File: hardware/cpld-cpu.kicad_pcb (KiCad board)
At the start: 4 copper layers, 259.1 x 198.1 mm, 435 parts, among them J1 Acc, J10 Page, J11 PC_H, J12 Conn_02x14_Odd_Even, J13 GPIO, J14 Conn_02x17_Odd_Even, J15 Conn_01x07, J16 Clock, J2 X, J3 IR, J4 AXM, J5 Dec, J6 AR, J7 ALU, J8 Index, J9 PC_L, SW1 BTN0, SW10 Step 8, SW11 S1, SW12 S3, SW2 BTN1, SW3 BTN2, SW4 Halt, SW5 Reset, SW6 Step 1, SW7 S0, SW8 S2, SW9 S4, U1 Acc, U10 RAM_Page, U11 PC_H, U12 CY62138FV30LL, U13 GPIO_RNG, U14 Clock, U2 X, U3 IR, U4 Multiplexer, U5 Decoder, U6 AR, U7 ALU, U8 RAM_Index, U9 PC_L

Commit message: Add logos and version
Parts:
- added H1: MountingHole, Mounting_Holes:MountingHole_4.3mm_M4, F.Cu at (15.2, 203.2)
- added H2: MountingHole, Mounting_Holes:MountingHole_4.3mm_M4, F.Cu at (15.2, 15.2)
- added H3: MountingHole, Mounting_Holes:MountingHole_4.3mm_M4, F.Cu at (264.2, 15.2)
- added H4: MountingHole, Mounting_Holes:MountingHole_4.3mm_M4, F.Cu at (264.2, 203.2)
- added S1: KicadLogo, Symbols:Symbol_KiCAD-Logo_CopperAndSilkScreenTop, F.Cu at (255.3, 61.0)
- added S2: OSHWLogo, CPLD_CPU_Symbols:OSHW-Logo2_14.6x12mm_Copper_Top, F.Cu at (237.5, 62.2)
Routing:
- added copper zone on F.Cu, net (none)
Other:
- board text added: "CPLD CPU"
- board text added: "https://github.com/jimmo/cpld-cpu/"
- board text added: "v1.0 2018-12-20"

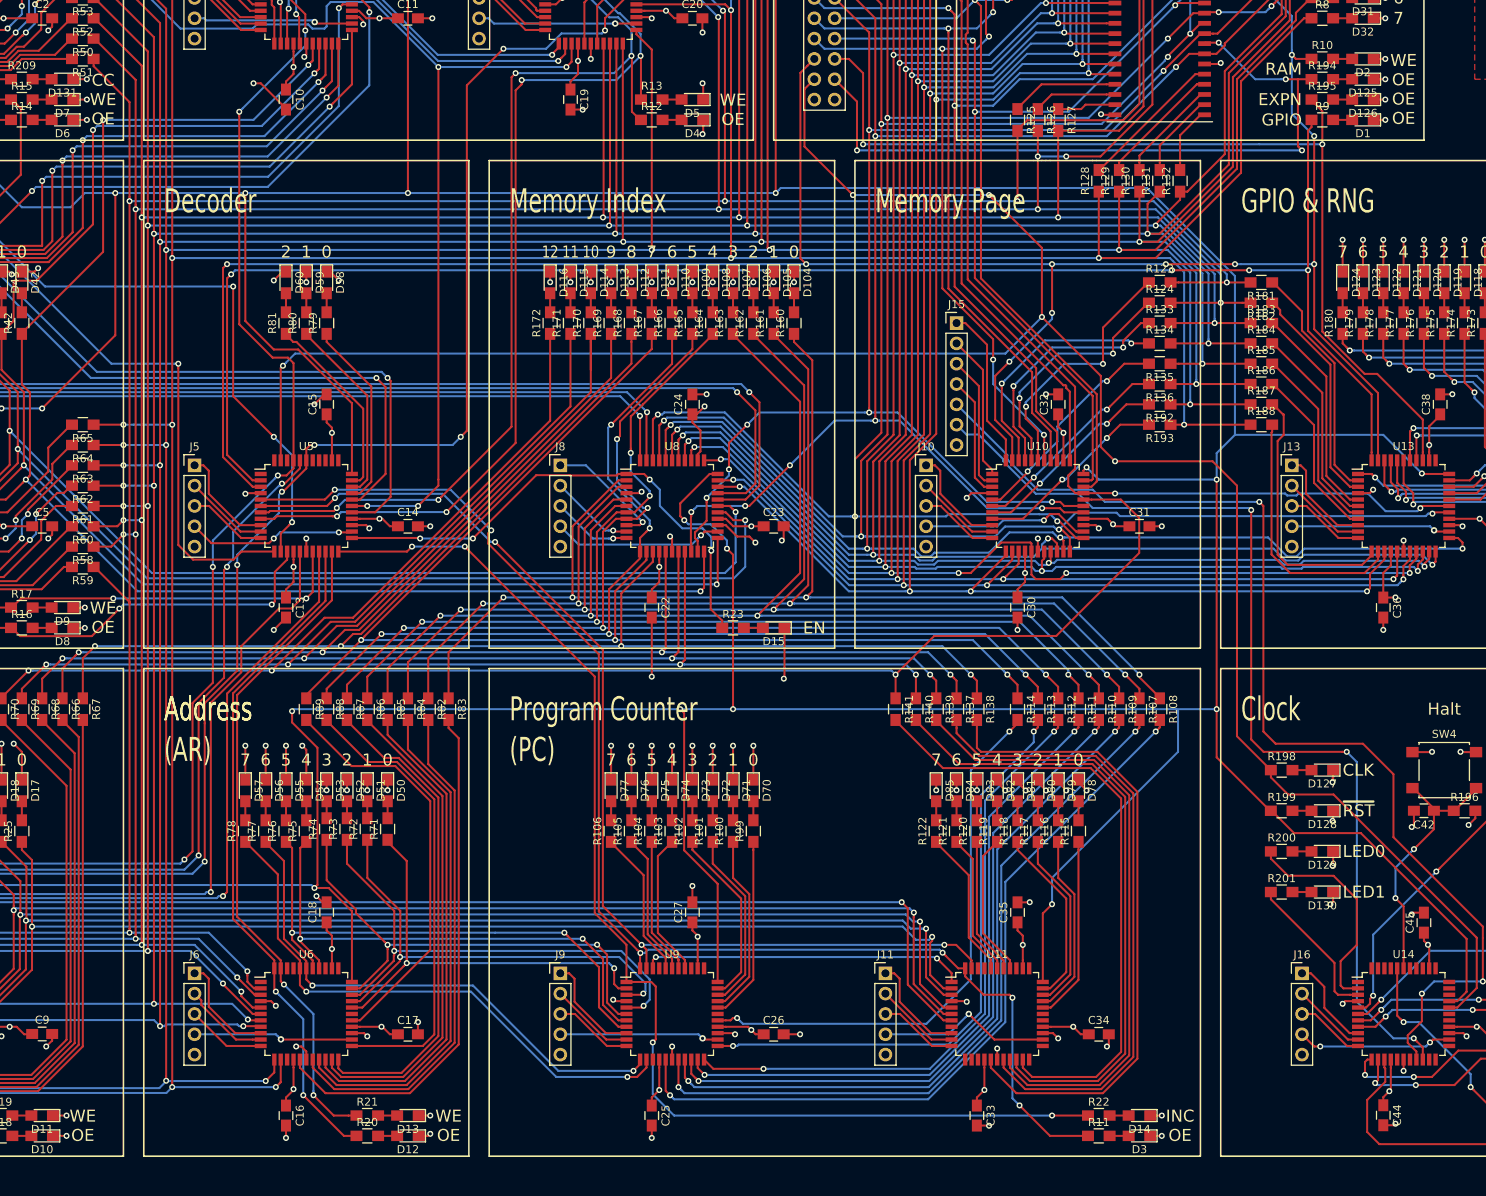
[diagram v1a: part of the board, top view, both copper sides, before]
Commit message: Name inverted nets correctly
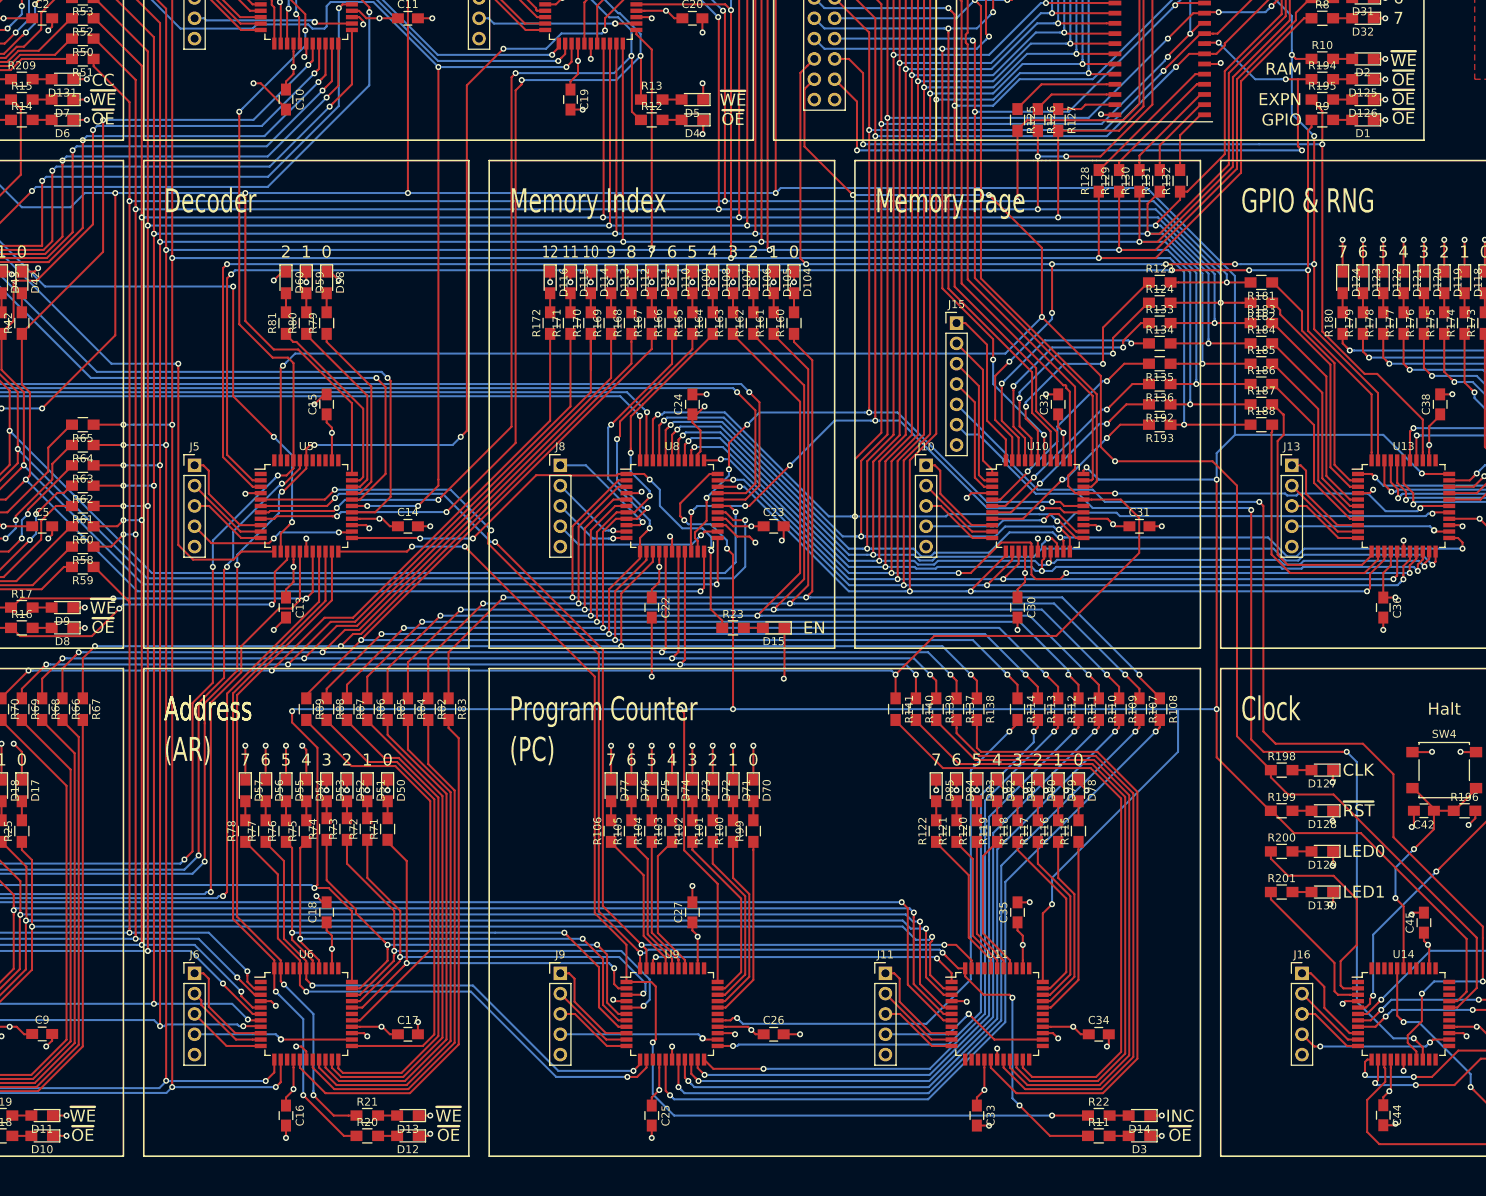
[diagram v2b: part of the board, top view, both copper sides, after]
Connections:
- net /ALU_OE renamed /ALU_~OE~
- net /ALU_WE renamed /ALU_~WE~
- net /AR_OE renamed /AR_~OE~
- net /AR_WE renamed /AR_~WE~
- net /A_OE renamed /A_~OE~
- net /A_WE renamed /A_~WE~
- net /DEV_OE renamed /DEV_~OE~
- net /GPIO_OE renamed /GPIO_~OE~
- net /IR_OE renamed /IR_~OE~
- net /IR_WE renamed /IR_~WE~
- net /PC_OE renamed /PC_~OE~
- net /PC_WE renamed /PC_~WE~
- net /RAM_OE renamed /RAM_~OE~
- net /RAM_WE renamed /RAM_~WE~
- net /RST renamed /~RST~
- net /X_OE renamed /X_~OE~
- net /X_WE renamed /X_~WE~
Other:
- board text added: "CC ~WE~ ~OE~"
- board text added: "INC ~OE~"
- board text added: "~WE~ ~OE~"
- board text added: "~WE~ ~OE~ ~OE~ ~OE~"
- board text removed: "CC WE OE"
- board text removed: "INC OE"
- board text removed: "WE OE"
- board text removed: "WE OE OE OE"

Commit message: Updated gerbers for seeed/jlcpcb
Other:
- rule pad_to_mask_clearance: 0.051 -> 0.05
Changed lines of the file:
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@@
     (pad_size 1.524 1.524)
     (pad_drill 0.762)
-    (pad_to_mask_clearance 0.051)
-    (solder_mask_min_width 0.25)
+    (pad_to_mask_clearance 0.05)
     (aux_axis_origin 0 0)
     (visible_elements FFFFFF7F)
     (pcbplotparams
-      (layerselection 0x010fc_ffffffff)
-      (usegerberextensions false)
+      (layerselection 0x010e8_ffffffff)
+      (usegerberextensions true)
       (usegerberattributes false)
       (usegerberadvancedattributes false)
@@
     (add_net /AR_~WE~)
     (add_net /A_CC)
+    (add_net /A_Z)
     (add_net /A_~OE~)
     (add_net /A_~WE~)
-    (add_net /A_Z)
     (add_net /BTN0)
     (add_net /BTN1)
@@
     (add_net /RAM_~OE~)
     (add_net /RAM_~WE~)
-    (add_net /~RST~)
     (add_net /X0)
     (add_net /X1)
@@
     (add_net /X_~OE~)
     (add_net /X_~WE~)
+    (add_net /~RST~)
     (add_net GND)
     (add_net "Net-(D1-Pad2)")
